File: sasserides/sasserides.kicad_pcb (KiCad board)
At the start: 2 copper layers, 170 x 80 mm, 134 parts, among them J1 Conn_02x16_Odd_Even, Q1 2N7002

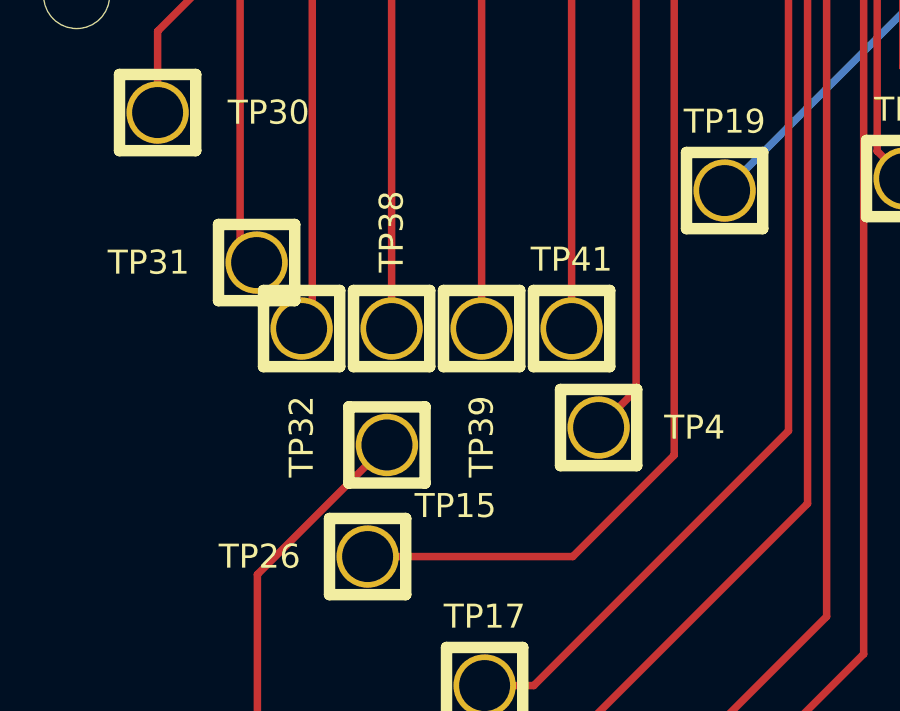
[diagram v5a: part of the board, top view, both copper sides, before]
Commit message: Clean up Sasserides silkscreen; Add meta data to all sheets
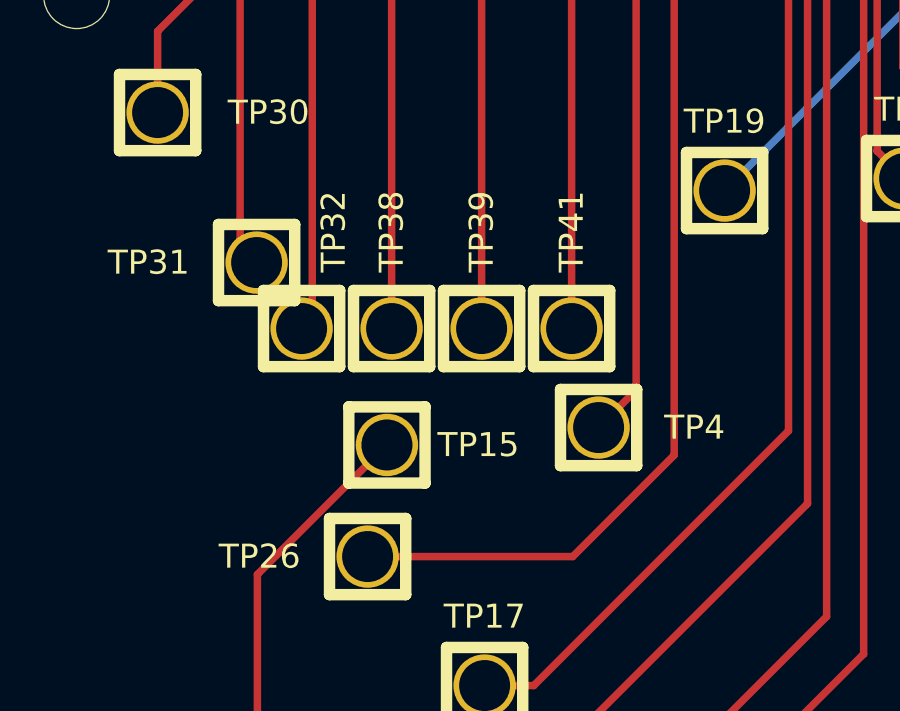
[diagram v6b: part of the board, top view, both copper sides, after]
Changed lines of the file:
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@@
   )
   (paper "A4")
+  (title_block
+    (title "Sasserides")
+    (date "${DATE}")
+    (rev "${VERSION}")
+    (company "Copyright 2023 Great Scott Gadgets")
+    (comment 1 "Licensed under the CERN-OHL-P v2")
+  )
   (layers
     (0 "F.Cu" signal)
@@
     )
   )
+  (property "DATE" "2023-05-24")
+  (property "VERSION" "r1.0.0")
   (net 0 "")
   (net 1 "Net-(D1-K)")
@@
     (property "ki_keywords" "test point tp")
     (attr through_hole)
-    (fp_text reference "TP39" (at 0 3.6 90) (layer "F.SilkS")
+    (fp_text reference "TP39" (at 0 -3.232 90) (layer "F.SilkS")
         (effects (font (size 0.8 0.8) (thickness 0.15)))
     )
@@
     (property "ki_keywords" "test point tp")
     (attr through_hole)
-    (fp_text reference "TP41" (at 0 -2.3 180) (layer "F.SilkS")
+    (fp_text reference "TP41" (at 0 -3.232 -90) (layer "F.SilkS")
         (effects (font (size 0.8 0.8) (thickness 0.15)))
     )
@@
     (property "ki_keywords" "test point tp")
     (attr through_hole)
-    (fp_text reference "TP15" (at 2.286 2.032) (layer "F.SilkS")
+    (fp_text reference "TP15" (at 3.048 0) (layer "F.SilkS")
         (effects (font (size 0.8 0.8) (thickness 0.15)))
     )
@@
     (property "ki_keywords" "test point tp")
     (attr through_hole)
-    (fp_text reference "TP32" (at 0 3.6 90) (layer "F.SilkS")
+    (fp_text reference "TP32" (at 1.066 -3.232 90) (layer "F.SilkS")
         (effects (font (size 0.8 0.8) (thickness 0.15)))
     )

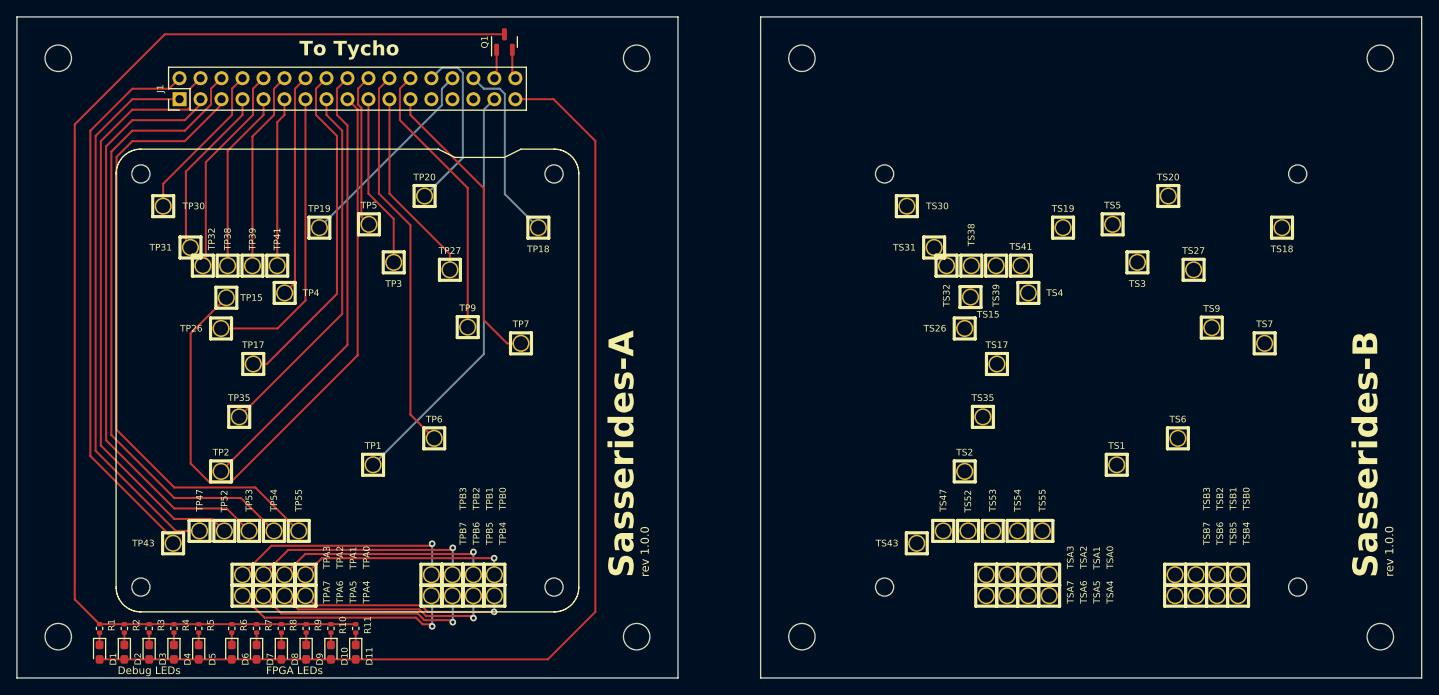
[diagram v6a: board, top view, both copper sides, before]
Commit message: Corrections to Sasserides A & B.
- Remove duplicate footprints for TP7, TP9 and TP15.
- Correct placement of TP9 and TP15.
- Adjust silkscreen placements on Sasserides B.
- Update date.
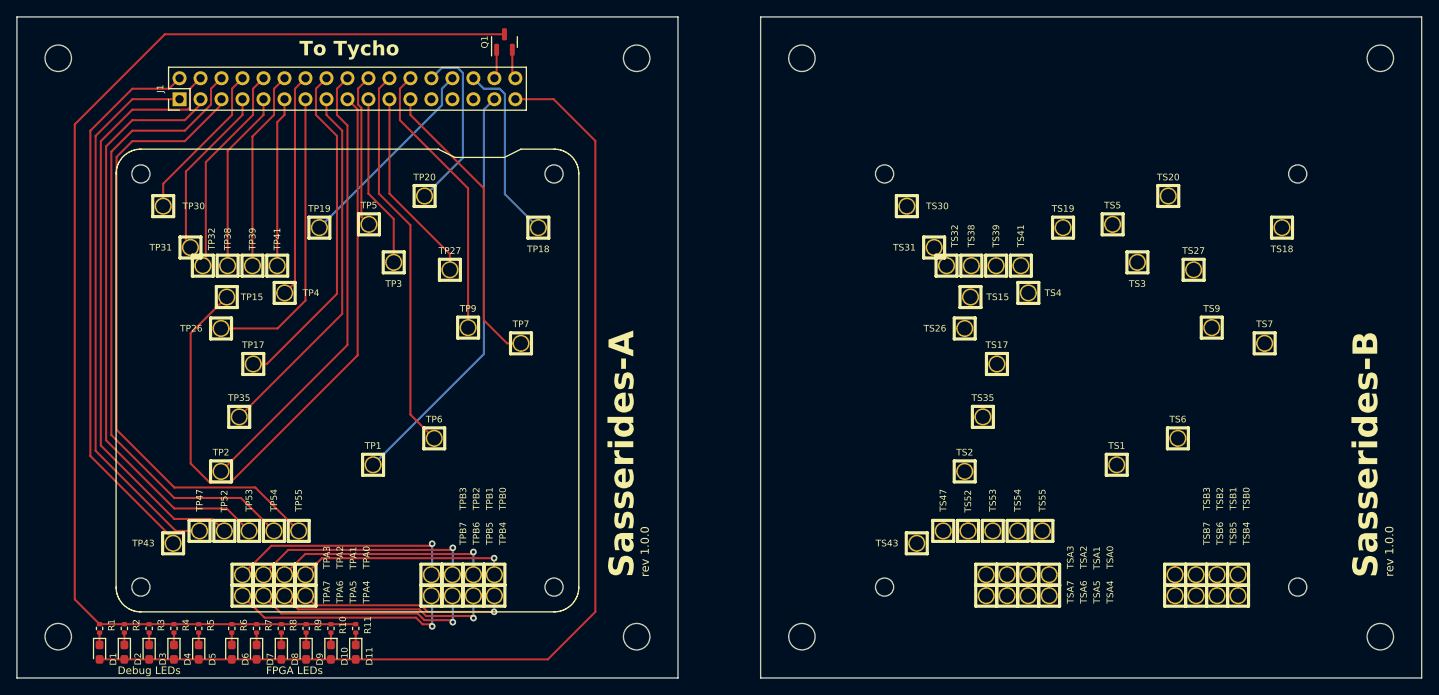
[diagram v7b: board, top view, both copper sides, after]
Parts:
- removed ? (x2): , 
- removed the TP15 at (85.4, 93.9)
- removed the TP7 at (121.0, 99.5)
- removed the TP9 at (114.6, 97.6)
- removed the TP9 at (204.6, 97.6)
- moved TP15 0.10 mm to (85.4, 93.9)
- moved TP9 0.08 mm to (114.6, 97.6)

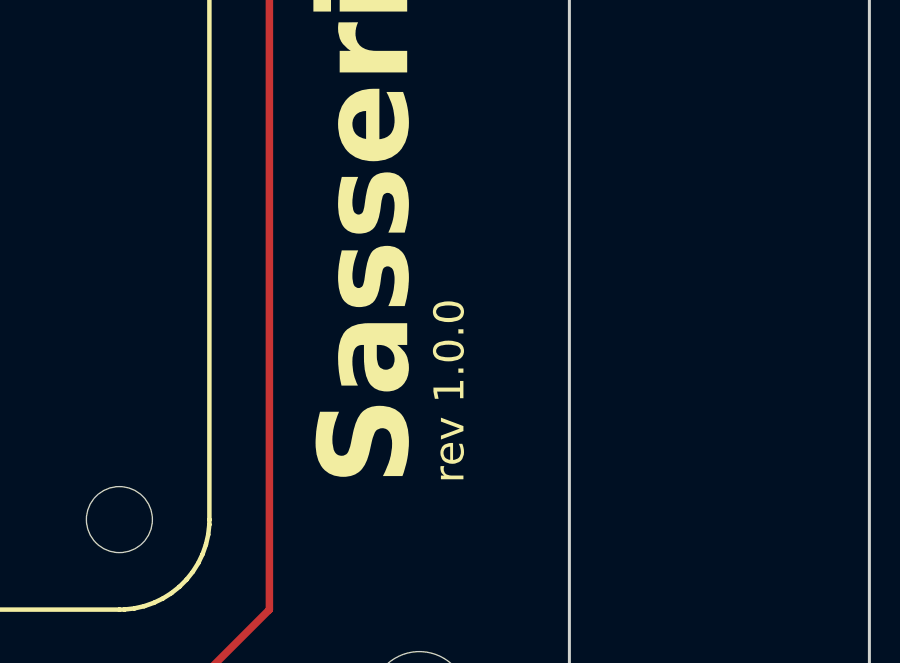
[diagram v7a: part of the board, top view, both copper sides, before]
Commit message: Change Sasserides-A version to 1.0.0+.
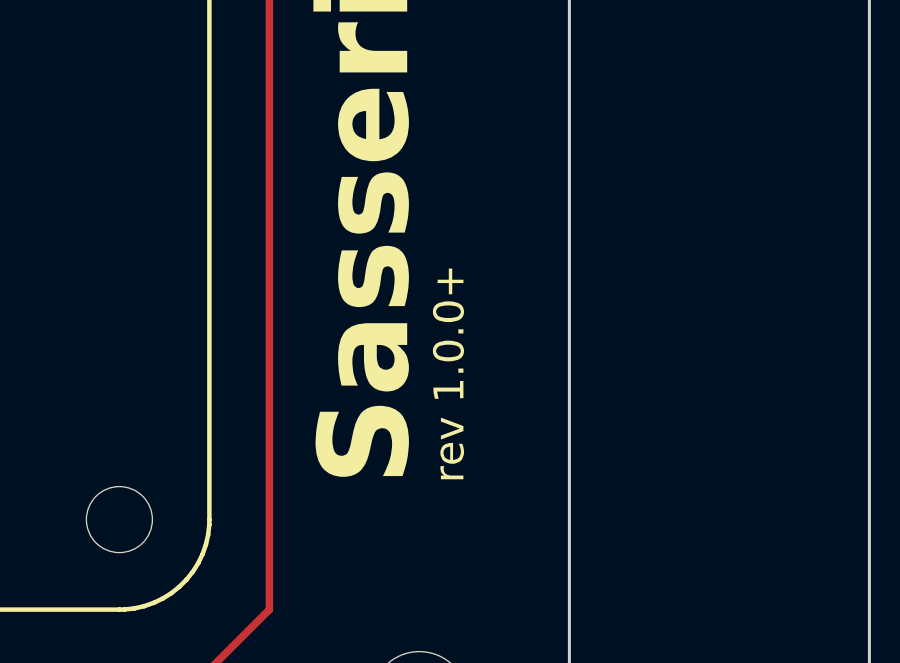
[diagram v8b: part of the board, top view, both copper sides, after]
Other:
- board text added: "rev 1.0.0+"
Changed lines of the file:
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@@
   )
   (property "DATE" "2023-05-25")
-  (property "VERSION" "r1.0.0")
+  (property "VERSION" "r1.0.0+")
   (net 0 "")
   (net 1 "Net-(D1-K)")
@@
   (gr_rect (start 60 60) (end 140 140)
     (stroke (width 0.1) (type default)) (fill none) (layer "Edge.Cuts"))
-  (gr_text "rev 1.0.0" (at 136.59 127.78 90) (layer "F.SilkS")
+  (gr_text "rev 1.0.0+" (at 136.59 127.78 90) (layer "F.SilkS")
     (effects (font (size 1 1) (thickness 0.15)) (justify left bottom))
   )
